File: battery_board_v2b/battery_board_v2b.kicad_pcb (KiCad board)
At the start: 4 copper layers, 88 x 94.5 mm, 120 parts, among them IC1 PCA9685PW,118, IC2 LT3652IMSE#PBF, IC3 PCT2075DP,118, J1 Face0, J11 CHARGE, J12 Foot0, J13 Foot1, J14 Foot2, J15 Foot3, J16 RBF, J17 BURN, J18 Bypass, J19 Heater, J2 Face1, J3 Face2, J4 Face3, J5 Face4, J6 FC_FACE, J7 5V Breakout, J8 ISS, K1 APAN3105, Q1 IRF7458, Q2 IRF7458, Q3 MBT2222ADW1T1, Q4 MBT2222ADW1T1, Q5 IRLML2803, Q6 NDS8434, Q7 MMBT2222AT, Q8 IRLML2803, Q9 NDS8434, U1 R5460N208AA, U2 TPS54226PWPRPWP14_2P31X2P46-L, U3 INA219AxD, U4 TCA9548APWR, U5 TPS7A4501DCQT, U6 INA219AxD, U7 1049, U8 1049

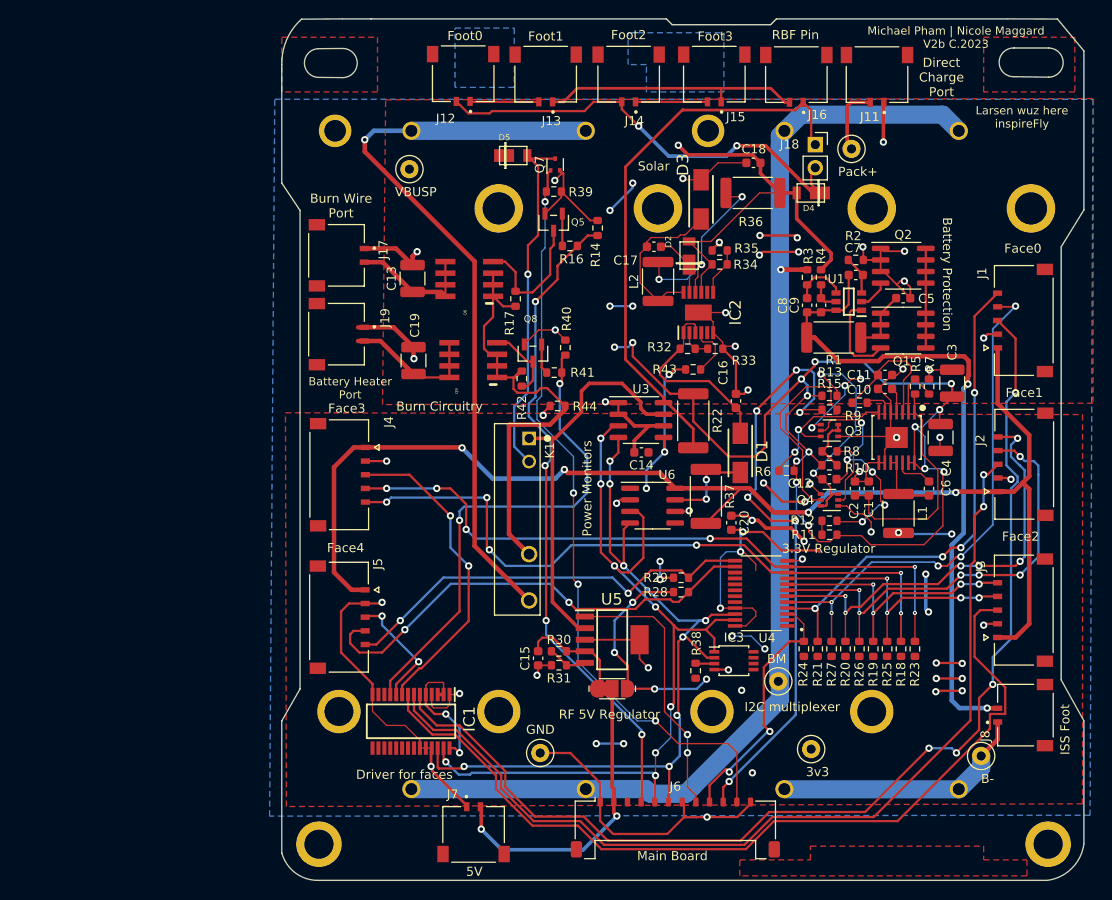
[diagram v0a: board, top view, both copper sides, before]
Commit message: Updated to add thermocouple driver onboard
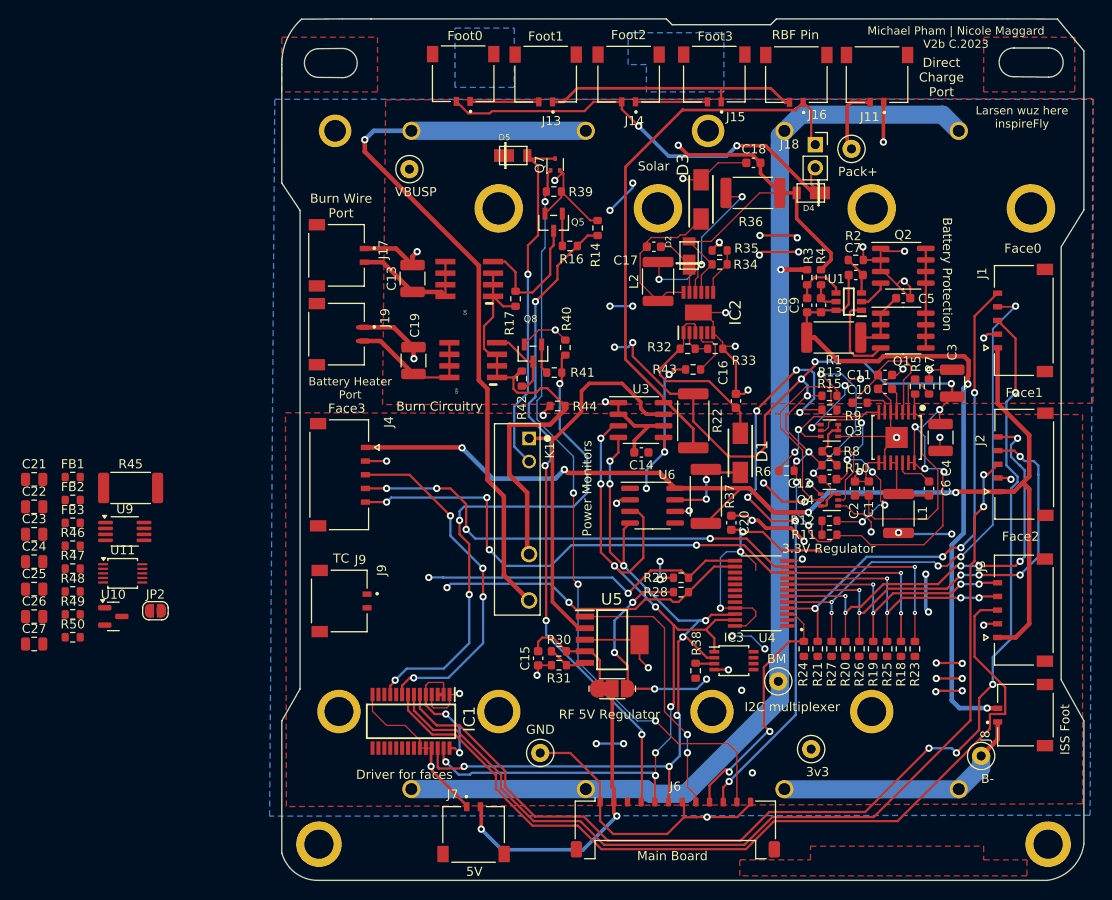
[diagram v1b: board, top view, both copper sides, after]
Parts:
- removed J5: Face4, MOLEX PICO LOCK 5 POS:MOLEX_5040500591
- added C21: 0.01uF, Capacitor_SMD:C_0805_2012Metric, F.Cu at (83.3, 91.5)
- added C22: 0.1uF, Capacitor_SMD:C_0805_2012Metric, F.Cu at (83.3, 94.5)
- added C23: 0.01uF, Capacitor_SMD:C_0805_2012Metric, F.Cu at (83.3, 97.5)
- added C24: 1uF, Capacitor_SMD:C_0805_2012Metric, F.Cu at (83.3, 100.5)
- added C25: 10uF, Capacitor_SMD:C_0805_2012Metric, F.Cu at (83.3, 103.5)
- added C26: 10uF, Capacitor_SMD:C_0805_2012Metric, F.Cu at (83.3, 106.6)
- added C27: 0.1uF, Capacitor_SMD:C_0805_2012Metric, F.Cu at (83.3, 109.6)
- added FB1: FerriteBead, Resistor_SMD:R_0603_1608Metric, F.Cu at (87.6, 91.3)
- added FB2: FerriteBead, Resistor_SMD:R_0603_1608Metric, F.Cu at (87.6, 93.8)
- added FB3: FerriteBead, Resistor_SMD:R_0603_1608Metric, F.Cu at (87.6, 96.3)
- added J9: TC, MOLEX PICO LOCK 2 POS:MOLEX_504050-0291, F.Cu at (116.8, 104.8)
- added JP2: SolderJumper_2_Open, Jumper:SolderJumper-2_P1.3mm_Open_RoundedPad1.0x1.5mm, F.Cu at (96.6, 105.9)
- added R45: 0.002, Resistor_SMD:R_2512_6332Metric, F.Cu at (93.9, 92.4)
- added R46: 1-MOhm, Resistor_SMD:R_0603_1608Metric, F.Cu at (87.6, 98.8)
- added R47: 100-Ohm, Resistor_SMD:R_0603_1608Metric, F.Cu at (87.6, 101.3)
- added R48: 100-Ohm, Resistor_SMD:R_0603_1608Metric, F.Cu at (87.6, 103.8)
- added R49: 1k, Resistor_SMD:R_0603_1608Metric, F.Cu at (87.6, 106.3)
- added R50: 10k-Ohm, Resistor_SMD:R_0603_1608Metric, F.Cu at (87.6, 108.8)
- added U10: TLVH431 DBZ SOT-23, Package_TO_SOT_SMD:SOT-23, F.Cu at (92.0, 106.5)
- added U11: ADS1015IDGS, Package_SO:TSSOP-10_3x3mm_P0.5mm, F.Cu at (93.0, 101.8)
- added U9: AD8495, Package_SO:MSOP-8_3x3mm_P0.65mm, F.Cu at (93.3, 97.2)
- renumbered J12 to J9
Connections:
- C7 pad 1: PACK- -> B-
- C8 pad 1: PACK- -> B-
- C9 pad 1: PACK- -> B-
- R1 pad 1: PACK- -> B-
- U1 pad 6: PACK- -> B-
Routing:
- net VSOLAR: track 140.8 -> 120.7 mm
- net F4_SCL: track 51.9 -> 35.1 mm
- net GND: track 271.2 -> 255.7 mm, vias 55 -> 54
- net F4_ENB: track 13.2 -> 0.00 mm, vias 2 -> 0
- net F4_SDA: track 46.5 -> 36.5 mm
- net F3_ENB: track 34.8 -> 38.6 mm, vias 2 -> 4
- net ENAB_HEATER: track 54.7 -> 58.0 mm, vias 2 -> 4
- net PACK-: vias 2 -> 0
- net B-: vias 0 -> 2
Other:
- board text added: "TC"
- board text removed: "Face4"

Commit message: Placed the thermocoupler circuitry on the board and modified schematic FOr the schematic I removed the adresse jumper ase we know which I2C adresse we are using.
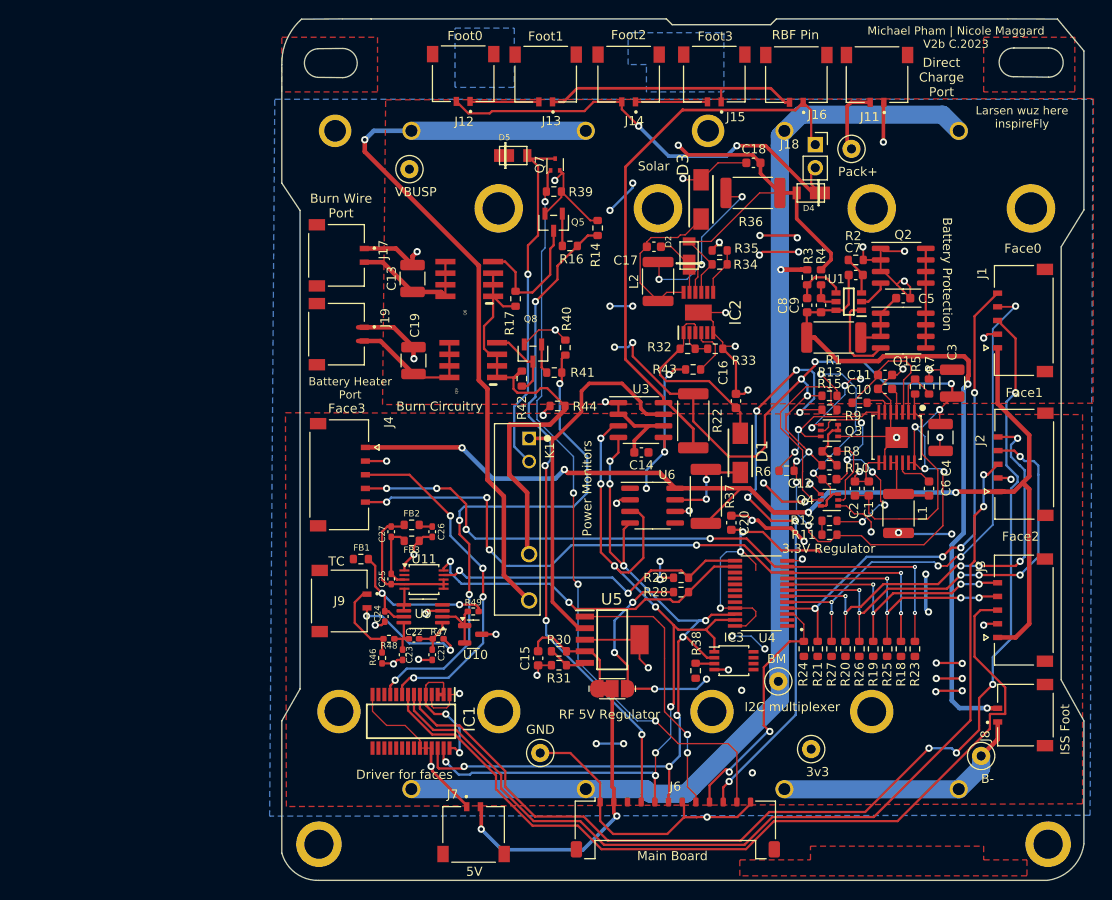
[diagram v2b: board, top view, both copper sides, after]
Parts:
- removed JP2: SolderJumper_2_Open, Jumper:SolderJumper-2_P1.3mm_Open_RoundedPad1.0x1.5mm
- removed R45: 0.002, Resistor_SMD:R_2512_6332Metric
- removed R50: 10k-Ohm, Resistor_SMD:R_0603_1608Metric
- C21, C22, C23, C24, C25, C26, C27: footprint Capacitor_SMD:C_0805_2012Metric -> Capacitor_SMD:C_0402_1005Metric_Pad0.74x0.62mm_HandSolder
- R46, R47, R48, R49: footprint Resistor_SMD:R_0603_1608Metric -> Resistor_SMD:R_0402_1005Metric_Pad0.72x0.64mm_HandSolder
- moved C21 47.7 mm to (127.0, 110.8), turned to 90 degrees
- moved C26 44.6 mm to (127.0, 97.2), turned to 90 degrees
- moved C22 44.1 mm to (125.0, 109.0)
- moved R49 43.9 mm to (131.5, 106.0)
- moved C23 42.5 mm to (123.8, 110.8), turned to -90 degrees
- moved C27 41.1 mm to (122.5, 97.2), turned to -90 degrees
- moved R47 40.8 mm to (127.7, 109.0), turned to 180 degrees
- moved U10 39.5 mm to (131.5, 108.5)
- moved C25 39.2 mm to (122.5, 102.4), turned to 90 degrees
- moved C24 38.9 mm to (121.8, 106.5), turned to -90 degrees
- moved FB2 37.3 mm to (124.8, 96.5)
- moved FB3 37.2 mm to (124.8, 98.2)
- moved R46 36.1 mm to (121.5, 111.1), turned to -90 degrees
- moved R48 35.1 mm to (122.2, 109.0), turned to 180 degrees
- moved U9 34.0 mm to (126.0, 106.2), turned to 180 degrees
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- renumbered J9 to J12
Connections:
- U11 pad 1: Net-(JP2-A) -> GND
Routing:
- net Net-(U9-+Vs): track 0.00 -> 20.5 mm, vias 0 -> 2
- net AVDD: track 0.00 -> 15.9 mm
- net GND: track 255.7 -> 270.0 mm, vias 54 -> 60
- net Net-(J9-Pin_2): track 0.00 -> 13.2 mm, vias 0 -> 2
- net Net-(J9-Pin_1): track 0.00 -> 9.41 mm
- net AGND: track 0.00 -> 7.36 mm
- net Net-(U10-K): track 0.00 -> 6.44 mm
- net Net-(U9-+IN): track 0.00 -> 4.95 mm
- net Net-(U9--IN): track 0.00 -> 4.91 mm
- net F4_SCL: track 35.1 -> 37.6 mm
- net OUT: track 0.00 -> 2.45 mm
- net +3V3: track 134.6 -> 136.1 mm
- net F4_SDA: track 36.5 -> 35.4 mm
